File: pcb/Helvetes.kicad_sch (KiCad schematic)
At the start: 13 parts

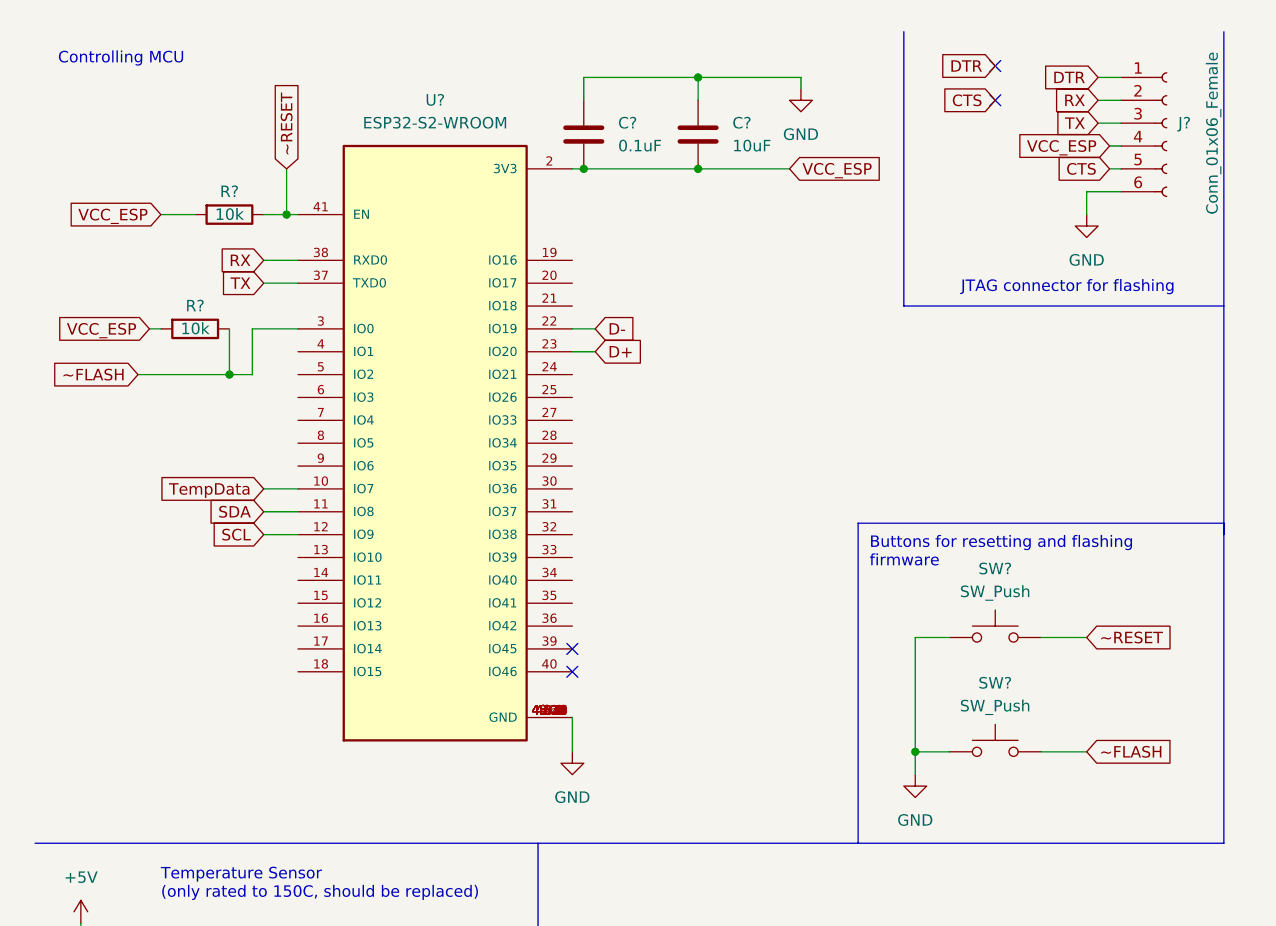
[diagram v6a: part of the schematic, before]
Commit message: :construction: Add an OLED display connector
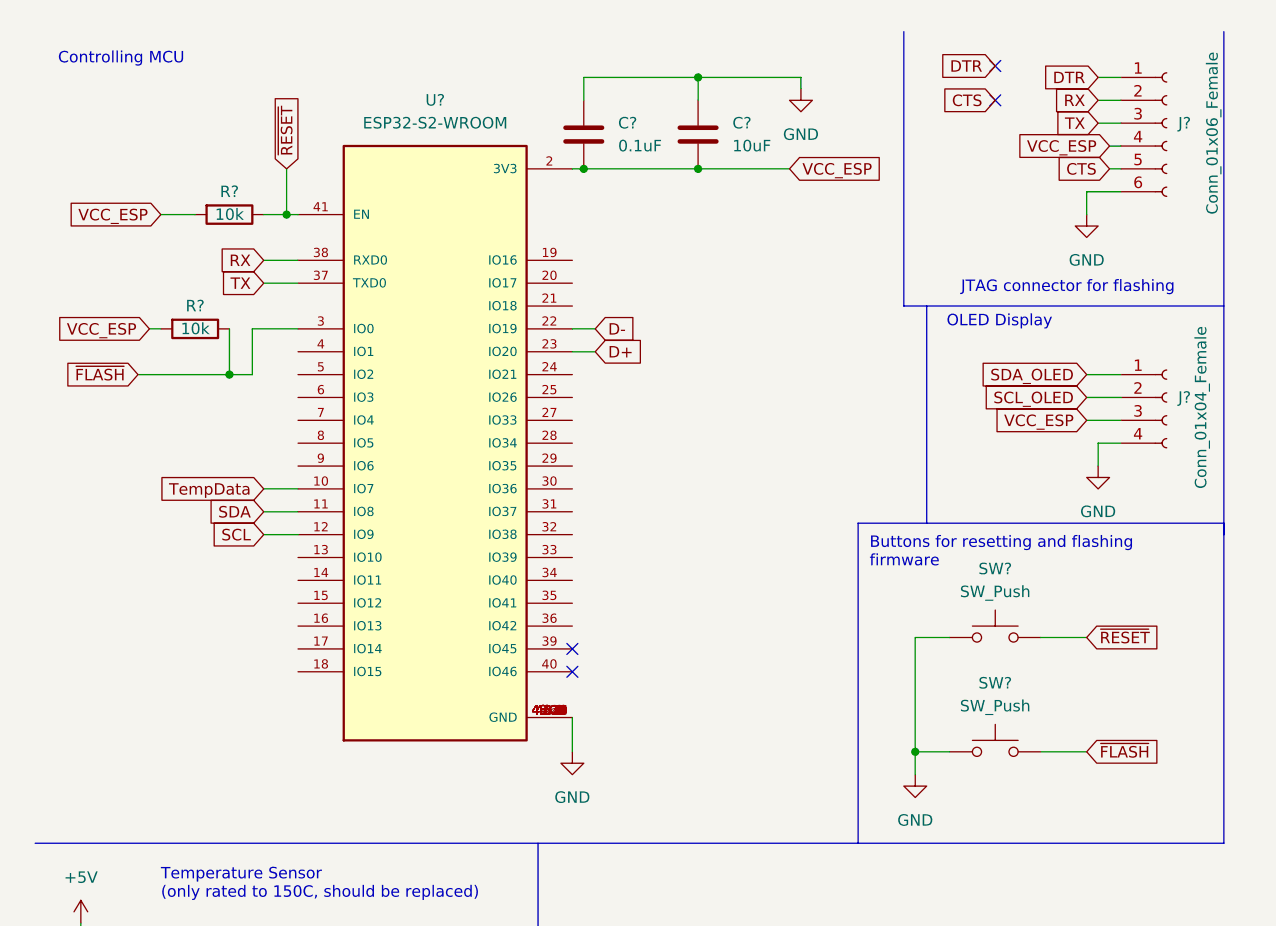
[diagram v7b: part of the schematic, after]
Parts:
- added J?: Conn_01x04_Female, symbol Connector:Conn_01x04_Female
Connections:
- net GND: now also J?.4 (Pin_4)
- net VCC_ESP: now also J?.3 (Pin_3)
- net ~FLASH renamed ~{FLASH}
- net ~RESET renamed ~{RESET}
- new net SCL_OLED: J?.2 (Pin_2)
- new net SDA_OLED: J?.1 (Pin_1)
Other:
- note added: "OLED Display"
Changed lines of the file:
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@@
+    (stroke (width 0) (type default) (color 0 0 0 0))
+  )
+  (wire (pts (xy 129.54 59.69) (xy 129.54 57.15))
     (stroke (width 0) (type default) (color 0 0 0 0))
   )
@@
     (stroke (width 0) (type default) (color 0 0 0 0))
   )
+  (wire (pts (xy 128.27 54.61) (xy 132.08 54.61))
+    (stroke (width 0) (type default) (color 0 0 0 0))
+  )
   (polyline (pts (xy 102.87 66.04) (xy 143.51 66.04))
     (stroke (width 0) (type default) (color 0 0 0 0))
@@
     (stroke (width 0) (type default) (color 0 0 0 0))
   )
+  (polyline (pts (xy 110.49 41.91) (xy 110.49 66.04))
+    (stroke (width 0) (type default) (color 0 0 0 0))
+  )
   (wire (pts (xy 63.5 172.72) (xy 63.5 167.64))
     (stroke (width 0) (type default) (color 0 0 0 0))
@@
     (stroke (width 0) (type default) (color 0 0 0 0))
   )
+  (wire (pts (xy 129.54 57.15) (xy 132.08 57.15))
+    (stroke (width 0) (type default) (color 0 0 0 0))
+  )
   (wire (pts (xy 71.12 44.45) (xy 73.66 44.45))
     (stroke (width 0) (type default) (color 0 0 0 0))
@@
     (stroke (width 0) (type default) (color 0 0 0 0))
   )
+  (wire (pts (xy 128.27 52.07) (xy 132.08 52.07))
+    (stroke (width 0) (type default) (color 0 0 0 0))
+  )
   (wire (pts (xy 129.54 19.05) (xy 132.08 19.05))
     (stroke (width 0) (type default) (color 0 0 0 0))
   )
+  (wire (pts (xy 128.27 49.53) (xy 132.08 49.53))
+    (stroke (width 0) (type default) (color 0 0 0 0))
+  )
   (wire (pts (xy 22.86 49.53) (xy 33.02 49.53))
     (stroke (width 0) (type default) (color 0 0 0 0))
@@
   (wire (pts (xy 59.69 177.8) (xy 63.5 177.8))
     (stroke (width 0) (type default) (color 0 0 0 0))
+  )
+  (text "OLED Display" (at 124.46 44.45 180)
+    (effects (font (size 1.27 1.27)) (justify right bottom))
   )
   (text "Controlling MCU" (at 13.97 15.24 0)
@@
     )
   )
-  (global_label "~RESET" (shape input) (at 128.27 78.74 0) (fields_autoplaced)
+  (global_label "~{RESET}" (shape input) (at 128.27 78.74 0) (fields_autoplaced)
     (effects (font (size 1.27 1.27)) (justify left))
-    (property "Intersheet References" "${INTERSHEET_REFS}" (id 0) (at 137.3355 78.6606 0)
+    (property "Intersheet References" "${INTERSHEET_REFS}" (id 0) (at 136.4283 78.6606 0)
       (effects (font (size 1.27 1.27)) (justify left) hide)
     )
@@
     )
   )
-  (global_label "~FLASH" (shape input) (at 128.27 91.44 0) (fields_autoplaced)
+  (global_label "~{FLASH}" (shape input) (at 128.27 91.44 0) (fields_autoplaced)
     (effects (font (size 1.27 1.27)) (justify left))
-    (property "Intersheet References" "${INTERSHEET_REFS}" (id 0) (at 137.3355 91.3606 0)
+    (property "Intersheet References" "${INTERSHEET_REFS}" (id 0) (at 136.4283 91.3606 0)
       (effects (font (size 1.27 1.27)) (justify left) hide)
     )
@@
     )
   )
-  (global_label "~FLASH" (shape input) (at 22.86 49.53 180) (fields_autoplaced)
-    (effects (font (size 1.27 1.27)) (justify right))
-    (property "Intersheet References" "${INTERSHEET_REFS}" (id 0) (at 13.7945 49.4506 0)
+  (global_label "~{FLASH}" (shape input) (at 22.86 49.53 180) (fields_autoplaced)
+    (effects (font (size 1.27 1.27)) (justify right))
+    (property "Intersheet References" "${INTERSHEET_REFS}" (id 0) (at 14.7017 49.4506 0)
       (effects (font (size 1.27 1.27)) (justify right) hide)
     )
@@
     )
   )
-  (global_label "~RESET" (shape input) (at 39.37 26.67 90) (fields_autoplaced)
+  (global_label "~{RESET}" (shape input) (at 39.37 26.67 90) (fields_autoplaced)
     (effects (font (size 1.27 1.27)) (justify left))
-    (property "Intersheet References" "${INTERSHEET_REFS}" (id 0) (at 39.2906 17.6045 90)
+    (property "Intersheet References" "${INTERSHEET_REFS}" (id 0) (at 39.2906 18.5117 90)
       (effects (font (size 1.27 1.27)) (justify left) hide)
     )
   )
+  (global_label "VCC_ESP" (shape input) (at 128.27 54.61 180) (fields_autoplaced)
+    (effects (font (size 1.27 1.27)) (justify right))
+    (property "Intersheet References" "${INTERSHEET_REFS}" (id 0) (at 117.6321 54.5306 0)
+      (effects (font (size 1.27 1.27)) (justify right) hide)
+    )
+  )
   (global_label "RX" (shape input) (at 129.54 19.05 180) (fields_autoplaced)
     (effects (font (size 1.27 1.27)) (justify right))
     (property "Intersheet References" "${INTERSHEET_REFS}" (id 0) (at 124.6474 18.9706 0)
+      (effects (font (size 1.27 1.27)) (justify right) hide)
+    )
+  )
+  (global_label "SCL_OLED" (shape input) (at 128.27 52.07 180) (fields_autoplaced)
+    (effects (font (size 1.27 1.27)) (justify right))
+    (property "Intersheet References" "${INTERSHEET_REFS}" (id 0) (at 116.604 51.9906 0)
+      (effects (font (size 1.27 1.27)) (justify right) hide)
+    )
+  )
+  (global_label "SDA_OLED" (shape input) (at 128.27 49.53 180) (fields_autoplaced)
+    (effects (font (size 1.27 1.27)) (justify right))
+    (property "Intersheet References" "${INTERSHEET_REFS}" (id 0) (at 116.5436 49.4506 0)
       (effects (font (size 1.27 1.27)) (justify right) hide)
     )
@@
     (pin "2")
   )
+  (symbol (lib_id "Connector:Conn_01x04_Female") (at 137.16 52.07 0) (unit 1)
+    (in_bom yes) (on_board yes)
+    (property "Reference" "J?" (id 0) (at 138.43 52.0699 0)
+      (effects (font (size 1.27 1.27)) (justify left))
+    )
+    (property "Value" "Conn_01x04_Female" (id 1) (at 140.97 62.23 90)
+      (effects (font (size 1.27 1.27)) (justify left))
+    )
+    (property "Footprint" "" (id 2) (at 137.16 52.07 0)
+      (effects (font (size 1.27 1.27)) hide)
+    )
+    (property "Datasheet" "~" (id 3) (at 137.16 52.07 0)
+      (effects (font (size 1.27 1.27)) hide)
+    )
+    (pin "1")
+    (pin "2")
+    (pin "3")
+    (pin "4")
+  )
+  (symbol (lib_id "power:GND") (at 129.54 59.69 0) (unit 1)
+    (in_bom yes) (on_board yes) (fields_autoplaced)
+    (property "Reference" "#PWR?" (id 0) (at 129.54 66.04 0)
+      (effects (font (size 1.27 1.27)) hide)
+    )
+    (property "Value" "GND" (id 1) (at 129.54 64.77 0))
+    (property "Footprint" "" (id 2) (at 129.54 59.69 0)
+      (effects (font (size 1.27 1.27)) hide)
+    )
+    (property "Datasheet" "" (id 3) (at 129.54 59.69 0)
+      (effects (font (size 1.27 1.27)) hide)
+    )
+    (pin "1")
+  )
   (symbol (lib_id "power:GND") (at 109.22 93.98 0) (unit 1)
     (in_bom yes) (on_board yes) (fields_autoplaced)
@@
   (symbol (lib_id "power:GND") (at 41.91 133.35 0) (unit 1)
     (in_bom yes) (on_board yes) (fields_autoplaced)
-    (property "Reference" "#PWR0103" (id 0) (at 41.91 139.7 0)
+    (property "Reference" "#PWR?" (id 0) (at 41.91 139.7 0)
       (effects (font (size 1.27 1.27)) hide)
     )
@@
   )
   (symbol_instances
-    (path "/ebad992a-bf26-4136-8d67-4e3bfe44b407"
-      (reference "#PWR0103") (unit 1) (value "GND") (footprint "")
-    )
     (path "/31aeb112-45f7-43a4-8b0c-158424f0d681"
       (reference "#PWR?") (unit 1) (value "GND") (footprint "")
@@
       (reference "#PWR?") (unit 1) (value "+5V") (footprint "")
     )
+    (path "/b25b7409-de94-449f-951b-1420fb12fbb7"
+      (reference "#PWR?") (unit 1) (value "GND") (footprint "")
+    )
     (path "/b827d638-1cf3-4911-a7dd-d2edd8dd103f"
       (reference "#PWR?") (unit 1) (value "GND") (footprint "")
     )
+    (path "/ebad992a-bf26-4136-8d67-4e3bfe44b407"
+      (reference "#PWR?") (unit 1) (value "GND") (footprint "")
+    )
     (path "/149fe5e3-c5de-4b00-a4da-9988610fa252"
       (reference "C?") (unit 1) (value "0.1uF") (footprint "")
@@
       (reference "J?") (unit 1) (value "Conn_01x06_Female") (footprint "")
     )
+    (path "/b03e4849-8256-41e0-845f-780dcce71f55"
+      (reference "J?") (unit 1) (value "Conn_01x04_Female") (footprint "")
+    )
     (path "/45d32487-e0d2-44ba-81a3-4a24d21e283c"
